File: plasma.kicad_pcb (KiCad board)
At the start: 2 copper layers, 27 parts, among them J1 Conn_01x08_Female, M1 1364_HV, Q1 MPSA42, Q2 MPSA42, Q3 MPSA42, Q4 MPSA42, Q5 MPSA42, Q6 MPSA42, U1 WeMos_D1_mini

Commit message: playing the routing game
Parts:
- moved R17 34.8 mm to (189.1, 61.8), turned to 90 degrees
- moved D1 29.2 mm to (213.6, 77.9), turned to 0 degrees
- moved Q4 21.3 mm to (197.2, 77.0), turned to 0 degrees
- moved Q1 14.8 mm to (197.1, 55.7), turned to 0 degrees
- moved M1 12.4 mm to (162.3, 54.3)
- moved R13 9.96 mm to (203.3, 74.7)
- moved R9 8.99 mm to (210.9, 78.8), turned to 180 degrees
- moved R10 7.64 mm to (219.8, 55.0), turned to 180 degrees
- moved Q2 7.32 mm to (197.1, 60.5), turned to 0 degrees
- moved R1 5.92 mm to (104.8, 71.6)
- moved R8 5.48 mm to (203.4, 70.8)
- moved Q5 5.26 mm to (197.2, 71.8), turned to 0 degrees
- moved Q3 5.16 mm to (197.1, 66.0), turned to 0 degrees
- moved Q6 4.75 mm to (205.9, 63.9), turned to 0 degrees
- moved R3 3.93 mm to (104.7, 80.3)
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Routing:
- net +5V: track 103.8 -> 143.3 mm
- net Net-(D1-Pad1): track 54.9 -> 26.8 mm
- net Net-(M1-Pad2): track 30.0 -> 6.26 mm
- net Net-(Q4-Pad2): track 109.0 -> 88.5 mm
- net Net-(Q1-Pad3): track 35.9 -> 16.7 mm
- net VSS: track 73.1 -> 54.9 mm
- net Net-(Q1-Pad2): track 79.4 -> 95.9 mm
- net /Phase3_Cathode: track 29.4 -> 43.8 mm
- net /Phase1_Cathode: track 37.9 -> 29.6 mm
- net Net-(Q5-Pad2): track 97.4 -> 90.1 mm
- net Net-(Q2-Pad2): track 87.5 -> 93.4 mm
- net /RESET: track 27.3 -> 31.2 mm
- net /Reset_Cathode: track 45.5 -> 49.1 mm
- net Net-(Q2-Pad3): track 10.7 -> 7.34 mm
- net /P2: track 25.8 -> 28.8 mm
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- added copper zone on B.Cu, net GND
- removed copper zone on F.Cu, net GND

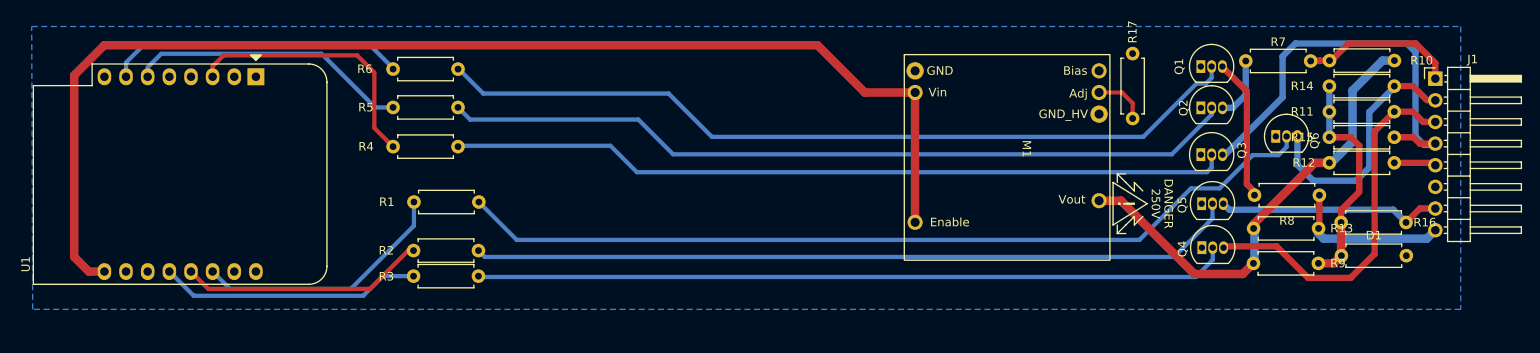
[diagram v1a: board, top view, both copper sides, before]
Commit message: added plasma vu-meter dimensions. trying to match them to the board
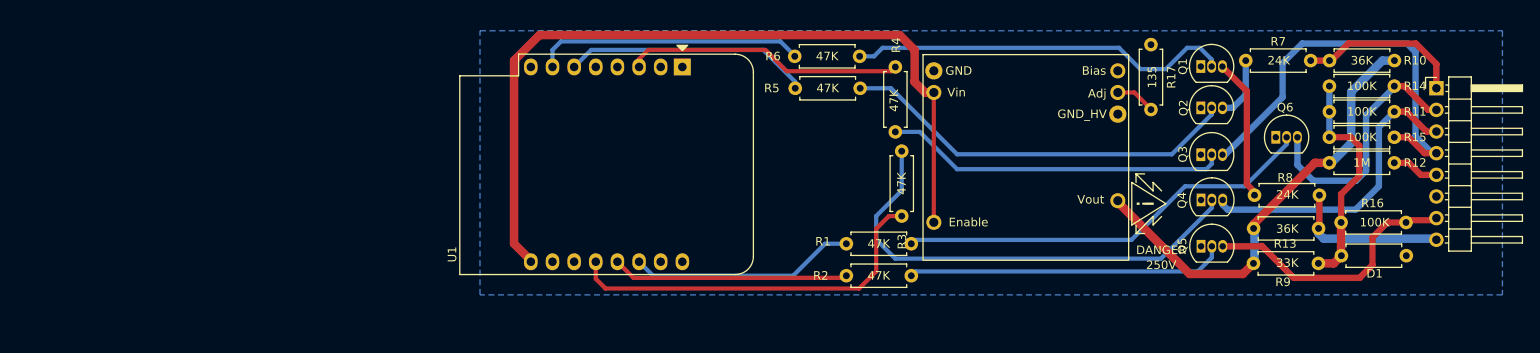
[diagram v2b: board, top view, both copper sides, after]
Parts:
- moved R4 59.7 mm to (161.2, 55.8), turned to -90 degrees
- moved R3 57.7 mm to (162.0, 73.2), turned to 90 degrees
- moved R1 51.0 mm to (155.5, 76.5)
- moved R2 50.9 mm to (155.5, 80.2)
- moved U1 50.1 mm to (136.2, 55.8)
- moved R5 47.3 mm to (149.5, 58.2)
- moved R6 47.2 mm to (149.4, 54.5)
- moved Q4 5.60 mm to (197.1, 71.4)
- moved Q5 5.00 mm to (197.1, 76.8)
- moved R17 2.39 mm to (191.2, 60.8)
- moved M1 2.20 mm to (164.5, 54.3)
- moved J1 1.13 mm to (224.8, 58.2)
- moved Q6 0.10 mm to (205.9, 64.0)
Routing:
- net Net-(Q6-Pad2): track 102.4 -> 49.7 mm
- net Net-(Q5-Pad2): track 90.1 -> 37.5 mm
- net Net-(Q3-Pad2): track 91.5 -> 40.3 mm
- net Net-(Q1-Pad2): track 95.9 -> 45.2 mm
- net +5V: track 143.3 -> 95.2 mm
- net Net-(Q2-Pad2): track 93.4 -> 47.2 mm
- net Net-(Q4-Pad2): track 88.5 -> 55.3 mm
- net /P3: track 30.8 -> 44.8 mm
- net /Phase3_Cathode: track 43.8 -> 36.1 mm
- net /Phase2_Cathode: track 26.9 -> 31.5 mm
- net /A1: track 33.2 -> 29.1 mm
- net /P1: track 30.3 -> 26.6 mm
- net /A2: track 35.1 -> 31.6 mm
- net VSS: track 54.9 -> 52.8 mm
- net /RESET: track 31.2 -> 32.7 mm
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
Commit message: moved the hole, made some gerbers
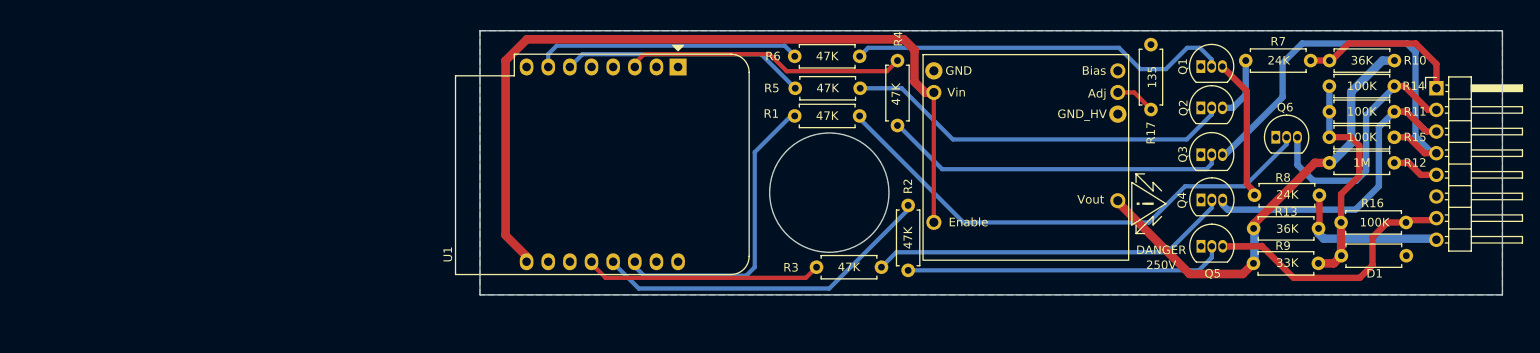
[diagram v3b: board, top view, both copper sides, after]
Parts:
- moved R1 16.2 mm to (149.4, 61.5)
- moved R3 11.7 mm to (152.0, 79.2), turned to 0 degrees
- moved R2 11.0 mm to (162.8, 72.0), turned to -90 degrees
- moved R4 0.79 mm to (161.5, 55.0)
- moved U1 0.50 mm to (135.8, 55.8)
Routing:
- net /P3: track 44.8 -> 27.8 mm
- net Net-(Q4-Pad2): track 55.3 -> 42.6 mm
- net /P2: track 27.8 -> 40.3 mm
- net Net-(Q6-Pad2): track 49.7 -> 60.1 mm
- net /P1: track 26.6 -> 35.5 mm
- net Net-(Q2-Pad2): track 47.2 -> 45.7 mm
- net +5V: track 95.2 -> 96.0 mm
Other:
- board outline added: 120 x 31 mm

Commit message: rounded PCB corners
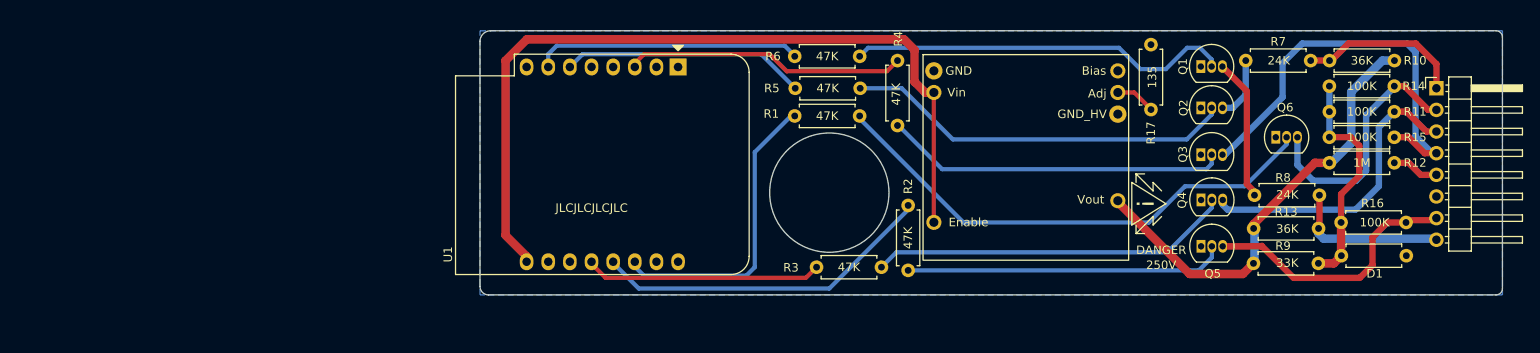
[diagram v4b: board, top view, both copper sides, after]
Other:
- outline, holes or cut-outs redrawn
- board text added: "JLCJLCJLCJLC"
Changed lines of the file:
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@@
   (gr_line (start 144 80) (end 163 80) (layer "Dwgs.User") (width 0.1))
   (gr_line (start 153.5 67) (end 153.5 51.5) (layer "Dwgs.User") (width 0.1))
-  (gr_rect (start 232.5 51.5) (end 112.5 82.5) (layer "Edge.Cuts") (width 0.1) (fill none))
+  (gr_arc (start 112.5 52.75) (mid 112.866117 51.866117) (end 113.75 51.5) (layer "Edge.Cuts") (width 0.05))
+  (gr_arc (start 232.5 81.75) (mid 232.28033 82.28033) (end 231.75 82.5) (layer "Edge.Cuts") (width 0.05))
+  (gr_line (start 232.5 81.75) (end 232.5 52.25) (layer "Edge.Cuts") (width 0.05))
+  (gr_arc (start 231.75 51.5) (mid 232.28033 51.71967) (end 232.5 52.25) (layer "Edge.Cuts") (width 0.05))
+  (gr_line (start 113.5 82.5) (end 231.75 82.5) (layer "Edge.Cuts") (width 0.05))
+  (gr_line (start 112.5 52.75) (end 112.5 81.5) (layer "Edge.Cuts") (width 0.05))
   (gr_circle (center 153.5 70.5) (end 160.5 70.5) (layer "Edge.Cuts") (width 0.1) (fill none))
+  (gr_line (start 231.75 51.5) (end 113.75 51.5) (layer "Edge.Cuts") (width 0.05))
+  (gr_arc (start 113.5 82.5) (mid 112.792893 82.207107) (end 112.5 81.5) (layer "Edge.Cuts") (width 0.05))
+  (gr_text "JLCJLCJLCJLC" (at 125.6 72.3) (layer "F.SilkS")
+    (effects (font (size 1 1) (thickness 0.15)))
+  )
   (segment (start 197 53.5) (end 198.37 54.87) (width 0.5) (layer "B.Cu") (net 2))
   (segment (start 157.06 54.5) (end 158.06 53.5) (width 0.5) (layer "B.Cu") (net 2))

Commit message: fine-tuning routing
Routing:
- net /Phase2_Cathode: track 31.5 -> 42.3 mm
- net /Phase1_Cathode: track 29.8 -> 27.8 mm
- net /Phase3_Cathode: track 35.7 -> 33.9 mm
- net Net-(Q6-Pad2): track 60.1 -> 60.8 mm
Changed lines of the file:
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@@
   (segment (start 199.646 60.548) (end 200.852 60.548) (width 0.75) (layer "B.Cu") (net 5))
   (segment (start 200.852 60.548) (end 202.376 59.024) (width 0.75) (layer "B.Cu") (net 5))
-  (segment (start 166.75 67.75) (end 197.75 67.75) (width 0.5) (layer "B.Cu") (net 6))
+  (segment (start 197.96 67.54) (end 198.376 67.124) (width 0.5) (layer "B.Cu") (net 6))
+  (segment (start 161.5 62.62) (end 161.62 62.62) (width 0.5) (layer "B.Cu") (net 6))
   (segment (start 198.376 67.124) (end 198.376 66.048) (width 0.5) (layer "B.Cu") (net 6))
-  (segment (start 161.62 62.62) (end 166.75 67.75) (width 0.5) (layer "B.Cu") (net 6))
-  (segment (start 197.75 67.75) (end 198.376 67.124) (width 0.5) (layer "B.Cu") (net 6))
-  (segment (start 161.5 62.62) (end 161.62 62.62) (width 0.5) (layer "B.Cu") (net 6))
+  (segment (start 166.54 67.54) (end 197.96 67.54) (width 0.5) (layer "B.Cu") (net 6))
+  (segment (start 161.62 62.62) (end 166.54 67.54) (width 0.5) (layer "B.Cu") (net 6))
   (segment (start 221.5 64) (end 223.37 65.87) (width 0.75) (layer "F.Cu") (net 7))
   (segment (start 219.81 64) (end 221.5 64) (width 0.75) (layer "F.Cu") (net 7))
@@
   (segment (start 223.58 63.33) (end 224.75 63.33) (width 0.75) (layer "F.Cu") (net 9))
   (segment (start 221.25 61) (end 223.58 63.33) (width 0.75) (layer "F.Cu") (net 9))
+  (segment (start 218 66.67) (end 212.17 72.5) (width 0.75) (layer "B.Cu") (net 9))
+  (segment (start 218 62.81) (end 218 66.67) (width 0.75) (layer "B.Cu") (net 9))
+  (segment (start 200.25 72.5) (end 199.67 71.92) (width 0.75) (layer "B.Cu") (net 9))
+  (segment (start 212.17 72.5) (end 200.25 72.5) (width 0.75) (layer "B.Cu") (net 9))
+  (segment (start 219.81 61) (end 218 62.81) (width 0.75) (layer "B.Cu") (net 9))
   (segment (start 199.67 71.92) (end 199.67 71.36) (width 0.75) (layer "B.Cu") (net 9))
-  (segment (start 219.81 61) (end 218 62.81) (width 0.75) (layer "B.Cu") (net 9))
-  (segment (start 215.25 72.5) (end 200.25 72.5) (width 0.75) (layer "B.Cu") (net 9))
-  (segment (start 200.25 72.5) (end 199.67 71.92) (width 0.75) (layer "B.Cu") (net 9))
-  (segment (start 218 69.75) (end 215.25 72.5) (width 0.75) (layer "B.Cu") (net 9))
-  (segment (start 218 62.81) (end 218 69.75) (width 0.75) (layer "B.Cu") (net 9))
   (segment (start 196.88 79.62) (end 198.4 78.1) (width 0.5) (layer "B.Cu") (net 10))
   (segment (start 198.4 78.1) (end 198.4 76.8) (width 0.5) (layer "B.Cu") (net 10))
   (segment (start 162.75 79.62) (end 196.88 79.62) (width 0.5) (layer "B.Cu") (net 10))
+  (segment (start 199.67 76.8) (end 204.2 76.8) (width 0.75) (layer "F.Cu") (net 11))
   (segment (start 224.75 73.49) (end 224.5 73.74) (width 0.75) (layer "F.Cu") (net 11))
+  (segment (start 226.87 73.49) (end 224.75 73.49) (width 0.75) (layer "F.Cu") (net 11))
   (segment (start 221.446 73.74) (end 221.186 74) (width 0.75) (layer "F.Cu") (net 11))
-  (segment (start 217.25 75.75) (end 217.25 79) (width 0.75) (layer "F.Cu") (net 11))
-  (segment (start 221.186 74) (end 219 74) (width 0.75) (layer "F.Cu") (net 11))
-  (segment (start 217.25 79) (end 215.75 80.5) (width 0.75) (layer "F.Cu") (net 11))
-  (segment (start 208 80.5) (end 204.25 76.75) (width 0.75) (layer "F.Cu") (net 11))
-  (segment (start 219 74) (end 217.25 75.75) (width 0.75) (layer "F.Cu") (net 11))
+  (segment (start 226.46 80.5) (end 227.96 79) (width 0.75) (layer "F.Cu") (net 11))
+  (segment (start 227.96 74.58) (end 226.87 73.49) (width 0.75) (layer "F.Cu") (net 11))
+  (segment (start 204.25 76.75) (end 208 80.5) (width 0.75) (layer "F.Cu") (net 11))
+  (segment (start 227.96 79) (end 227.96 74.58) (width 0.75) (layer "F.Cu") (net 11))
+  (segment (start 208 80.5) (end 226.46 80.5) (width 0.75) (layer "F.Cu") (net 11))
   (segment (start 224.5 73.74) (end 221.446 73.74) (width 0.75) (layer "F.Cu") (net 11))
-  (segment (start 215.75 80.5) (end 208 80.5) (width 0.75) (layer "F.Cu") (net 11))
-  (segment (start 204.25 76.75) (end 204.2 76.8) (width 0.75) (layer "F.Cu") (net 11))
-  (segment (start 204.2 76.8) (end 199.67 76.8) (width 0.75) (layer "F.Cu") (net 11))
-  (segment (start 157.06 61.81) (end 169.25 74) (width 0.5) (layer "B.Cu") (net 12))
+  (segment (start 204.2 76.8) (end 204.25 76.75) (width 0.75) (layer "F.Cu") (net 11))
+  (segment (start 202.44 69.56) (end 207.17 64.83) (width 0.5) (layer "B.Cu") (net 12))
+  (segment (start 170.08 74.83) (end 190.83 74.83) (width 0.5) (layer "B.Cu") (net 12))
+  (segment (start 157.06 61.81) (end 170.08 74.83) (width 0.5) (layer "B.Cu") (net 12))
+  (segment (start 196.1 69.56) (end 202.44 69.56) (width 0.5) (layer "B.Cu") (net 12))
+  (segment (start 190.83 74.83) (end 196.1 69.56) (width 0.5) (layer "B.Cu") (net 12))
   (segment (start 157.06 61.5) (end 157.06 61.81) (width 0.5) (layer "B.Cu") (net 12))
-  (segment (start 202.25 69.75) (end 207.17 64.83) (width 0.5) (layer "B.Cu") (net 12))
-  (segment (start 191 74) (end 195.25 69.75) (width 0.5) (layer "B.Cu") (net 12))
-  (segment (start 169.25 74) (end 191 74) (width 0.5) (layer "B.Cu") (net 12))
   (segment (start 207.17 64.83) (end 207.17 64) (width 0.5) (layer "B.Cu") (net 12))
-  (segment (start 195.25 69.75) (end 202.25 69.75) (width 0.5) (layer "B.Cu") (net 12))
   (segment (start 223.79 60.79) (end 224.75 60.79) (width 0.75) (layer "F.Cu") (net 13))
   (segment (start 219.81 58) (end 221 58) (width 0.75) (layer "F.Cu") (net 13))
   (segment (start 221 58) (end 223.79 60.79) (width 0.75) (layer "F.Cu") (net 13))
-  (segment (start 208.44 67.24) (end 210.3 69.1) (width 0.75) (layer "B.Cu") (net 13))
   (segment (start 216.5 61.424) (end 219.81 58.114) (width 0.75) (layer "B.Cu") (net 13))
-  (segment (start 216.5 67.924) (end 216.5 61.424) (width 0.75) (layer "B.Cu") (net 13))
-  (segment (start 208.44 64) (end 208.44 67.24) (width 0.75) (layer "B.Cu") (net 13))
-  (segment (start 215.324 69.1) (end 216.5 67.924) (width 0.75) (layer "B.Cu") (net 13))
-  (segment (start 210.3 69.1) (end 215.324 69.1) (width 0.75) (layer "B.Cu") (net 13))
+  (segment (start 213.00787 68.974511) (end 216.5 65.482381) (width 0.75) (layer "B.Cu") (net 13))
+  (segment (start 208.44 66.44) (end 210.974511 68.974511) (width 0.75) (layer "B.Cu") (net 13))
+  (segment (start 216.5 65.482381) (end 216.5 61.424) (width 0.75) (layer "B.Cu") (net 13))
+  (segment (start 208.44 64) (end 208.44 66.44) (width 0.75) (layer "B.Cu") (net 13))
+  (segment (start 210.974511 68.974511) (end 213.00787 68.974511) (width 0.75) (layer "B.Cu") (net 13))
   (segment (start 146.5 54.25) (end 148.5 56.25) (width 0.5) (layer "F.Cu") (net 16))
   (segment (start 130.67 55.75) (end 130.67 55.33) (width 0.5) (layer "F.Cu") (net 16))
@@
   (segment (start 149.44 61.5) (end 149 61.5) (width 0.5) (layer "B.Cu") (net 26))
   (segment (start 215.7 68.55) (end 215.7 65) (width 0.75) (layer "F.Cu") (net 29))
-  (segment (start 210.9 78.8) (end 212.7 78.8) (width 1) (layer "F.Cu") (net 29))
-  (segment (start 213.566 77.866) (end 213.6 77.9) (width 1) (layer "F.Cu") (net 29))
-  (segment (start 212.7 78.8) (end 213.6 77.9) (width 1) (layer "F.Cu") (net 29))
   (segment (start 213.566 70.684) (end 215.7 68.55) (width 0.75) (layer "F.Cu") (net 29))
   (segment (start 215.7 65) (end 214.7 64) (width 0.75) (layer "F.Cu") (net 29))
   (segment (start 213.566 74) (end 213.566 70.684) (width 0.75) (layer "F.Cu") (net 29))
-  (segment (start 213.566 74) (end 213.566 77.866) (width 1) (layer "F.Cu") (net 29))
   (segment (start 214.7 64) (end 212.19 64) (width 0.75) (layer "F.Cu") (net 29))
+  (segment (start 212.7 78.8) (end 213.6 77.9) (width 1) (layer "B.Cu") (net 29))
+  (segment (start 213.6 74.034) (end 213.566 74) (width 1) (layer "B.Cu") (net 29))
+  (segment (start 210.9 78.8) (end 212.7 78.8) (width 1) (layer "B.Cu") (net 29))
   (segment (start 212.19 58) (end 212.19 61) (width 0.75) (layer "B.Cu") (net 29))
   (segment (start 212.19 61) (end 212.19 64) (width 0.75) (layer "B.Cu") (net 29))
+  (segment (start 213.6 77.9) (end 213.6 74.034) (width 1) (layer "B.Cu") (net 29))
   (segment (start 222.337343 53) (end 224.75 55.412657) (width 0.75) (layer "F.Cu") (net 30))
   (segment (start 212.206 55) (end 212.424 55) (width 0.75) (layer "F.Cu") (net 30))
@@
   (segment (start 221.5 67) (end 222.91 68.41) (width 0.75) (layer "F.Cu") (net 31))
   (segment (start 219.81 67) (end 221.5 67) (width 0.75) (layer "F.Cu") (net 31))
+  (segment (start 224.75 76.03) (end 212.25 76.03) (width 1) (layer "F.Cu") (net 32))
   (segment (start 211.02 74.6) (end 210.92 74.7) (width 0.75) (layer "F.Cu") (net 32))
+  (segment (start 212.25 76.03) (end 210.92 74.7) (width 1) (layer "F.Cu") (net 32))
   (segment (start 211.02 70.8) (end 211.02 74.6) (width 0.75) (layer "F.Cu") (net 32))
-  (segment (start 210.92 74.7) (end 210.92 75.296) (width 1) (layer "B.Cu") (net 32))
-  (segment (start 224.62 75.9) (end 224.75 76.03) (width 1) (layer "B.Cu") (net 32))
-  (segment (start 211.524 75.9) (end 224.62 75.9) (width 1) (layer "B.Cu") (net 32))
-  (segment (start 210.92 75.296) (end 211.524 75.9) (width 1) (layer "B.Cu") (net 32))
   (segment (start 203.3 74.2) (end 203.3 74.7) (width 1) (layer "F.Cu") (net 33))
   (segment (start 212.19 67) (end 210.5 67) (width 1) (layer "F.Cu") (net 33))
